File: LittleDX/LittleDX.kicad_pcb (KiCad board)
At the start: 2 copper layers, 140 x 88 mm, 228 parts, among them J1 POWER, J10 PA6, J11 AudioJack2_Dual_Ground_Switch, J12 Conn_Coaxial, J13 Conn_01x01, J14 Conn_01x01, J15 Conn_01x01, J16 Conn_01x01, J17 Filt1, J18 Filt2, J19 AudioJack2_Dual_Ground_Switch, J2 Barrel_Jack, J20 Conn_01x02, J22 Conn_01x02, J23 Conn_01x01, J24 TRANSMIT, J25 Conn_01x04, J26 USB_B, J27 Conn_01x04, J3 Conn_01x01, J4 Conn_01x01, J5 CONFIG, J6 Conn_01x01, J7 Conn_01x01, J8 AudioJack2_Dual_Ground_Switch, J9 PB9, P1 Mini-DIN_6pins_ver4, Q12 MMBT2222, Q13 SS8550, Q14 MMBT3904, Q15 NC, Q3 2N7000, Q4 MMBT3904, Q5 NC, Q6 2N7000, Q7 2N7000, Q8 SS8550, Q9 2N7000, SW1 SW_Push, SW2 SW_Push, SW3 SW_Push, SW4 SW_Push, SW5 SW_Push, SW6 SW_Push, T3 Current, T4 Common-Mode Choke, U1 STM32F103C8Tx, U2 LM78M05_TO252, U3 LM386, U4 AMS1117-3.3, U5 LM358, U6 SI5351A, U7 MicroSD_SPI_CD, U8 Si4735-D60-GU, Y1 8 MHz, Y2 32.768 kHz, Y3 25 MHz

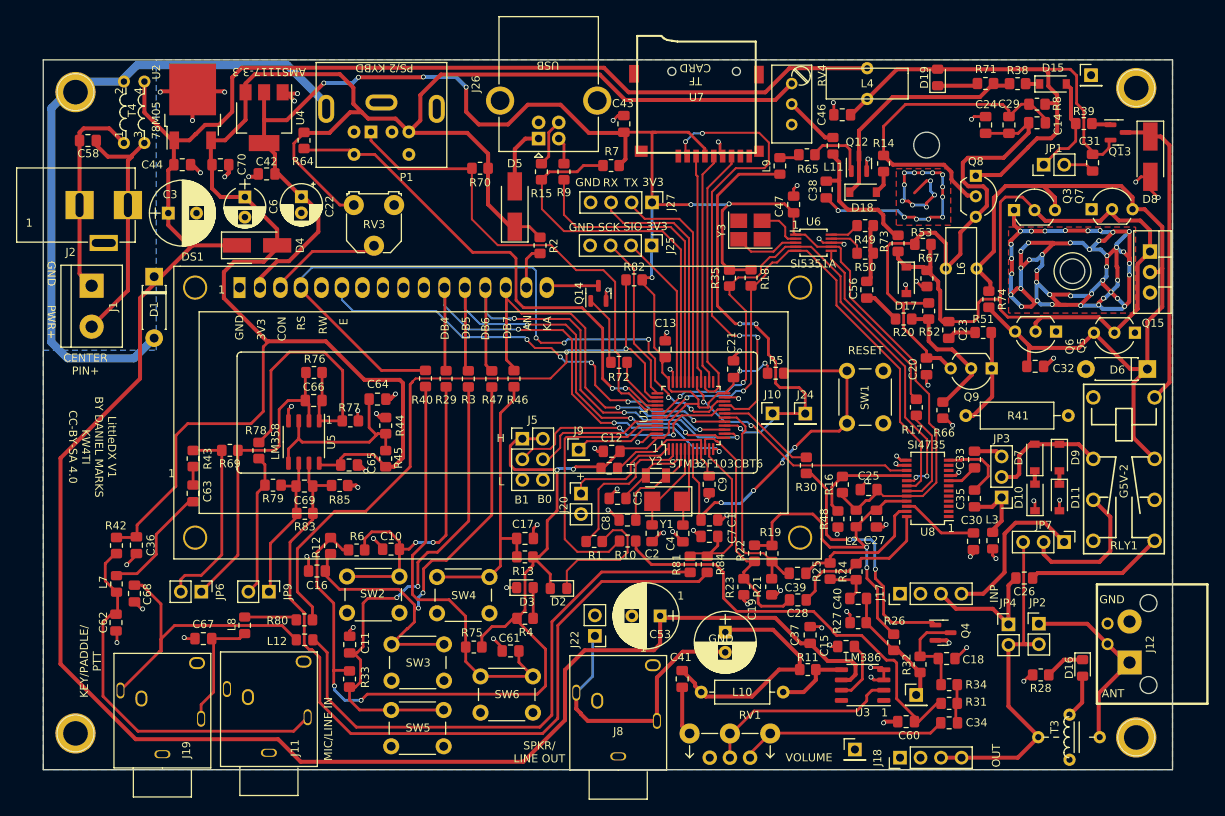
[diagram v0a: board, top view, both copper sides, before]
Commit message: Small moving around of components
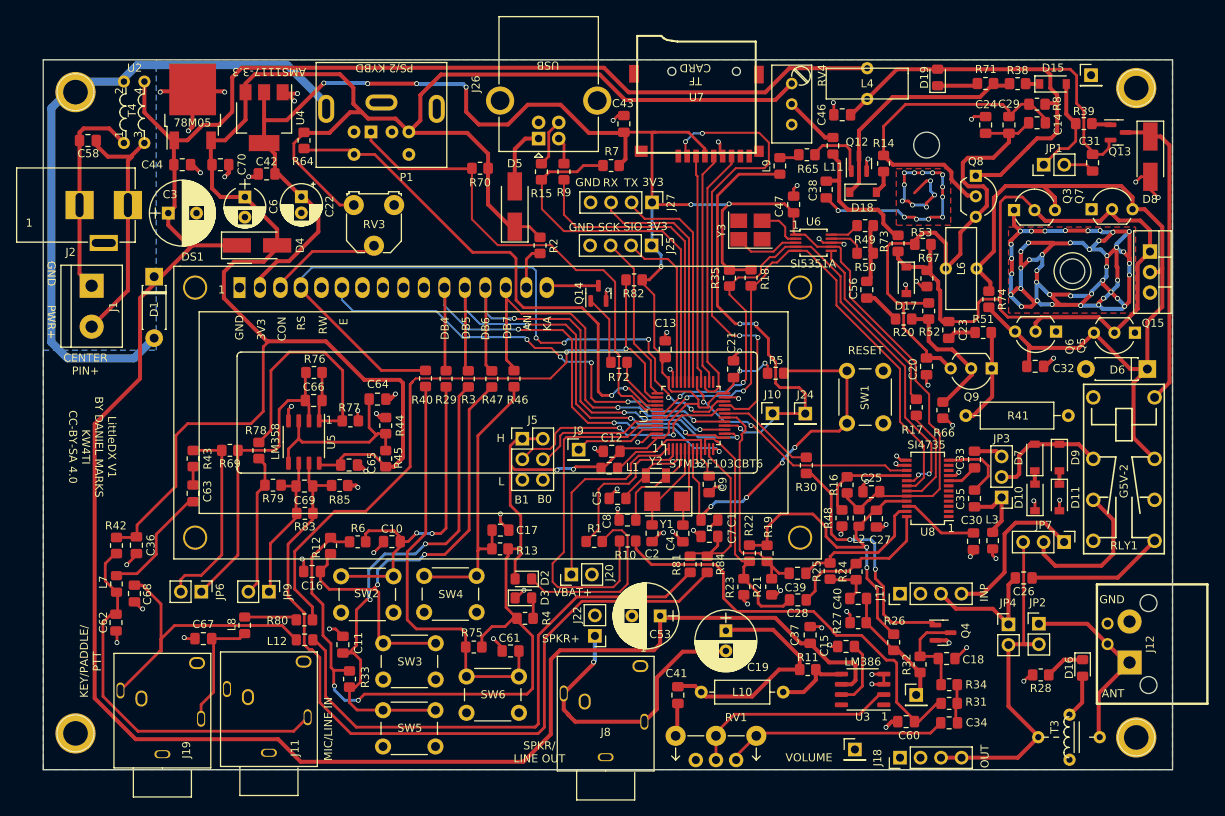
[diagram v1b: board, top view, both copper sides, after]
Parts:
- moved J20 10.1 mm to (115.5, 120.8), turned to 90 degrees
- moved D2 4.52 mm to (109.5, 121.3)
- moved R13 3.24 mm to (106.6, 117.6)
- moved C17 3.22 mm to (106.7, 115.3)
- moved C41 2.07 mm to (128.7, 135.8)
- moved RV1 1.75 mm to (133.4, 143.8)
- moved SW6 1.74 mm to (102.5, 133.4)
- moved SW4 1.60 mm to (97.2, 121.0)
- moved J8 1.56 mm to (119.7, 145.2)
- moved D3 1.29 mm to (109.5, 123.7)
- moved SW3 1.04 mm to (92.2, 129.3)
- moved R6 1.02 mm to (89.0, 116.8)
- moved SW5 1.02 mm to (92.1, 137.6)
- moved C10 0.94 mm to (93.2, 116.7)
- moved C11 0.84 mm to (87.2, 129.5)
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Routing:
- net BEEPOUT: track 32.6 -> 44.4 mm
- net Net-(U1-Pad1): track 14.7 -> 25.2 mm
- net Net-(D2-Pad1): track 16.9 -> 23.1 mm
- net Net-(C14-Pad1): track 69.3 -> 66.2 mm
- net PS2CLK: track 63.7 -> 65.7 mm
- net Net-(C34-Pad2): track 25.7 -> 27.6 mm
- net SPKR: track 35.9 -> 37.6 mm, vias 0 -> 1
- net Net-(J25-Pad2): track 19.3 -> 21.0 mm
- net Net-(RV1-Pad2): track 24.7 -> 26.1 mm
- net +3.3V: track 371.9 -> 370.4 mm
- net Net-(C16-Pad2): track 60.9 -> 59.7 mm
- net E: track 56.6 -> 57.8 mm
- net Net-(D3-Pad2): track 3.82 -> 2.62 mm
- net Net-(JP7-Pad2): track 17.9 -> 19.1 mm
- net GND: track 379.3 -> 380.4 mm
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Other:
- board text added: "SPKR+"
- board text added: "VBAT+"
- board text removed: "+"

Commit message: JLCPCB version 2
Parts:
- removed L1: 100 uH, Inductor_SMD:L_0805_2012Metric_Pad1.15x1.40mm_HandSolder
- added C45: 100 nF, Capacitor_SMD:C_0805_2012Metric_Pad1.18x1.45mm_HandSolder, F.Cu at (107.3, 120.3)
- added C48: 10 uF, Capacitor_SMD:C_0805_2012Metric_Pad1.18x1.45mm_HandSolder, F.Cu at (151.1, 140.1)
- added C49: 100 nF, Capacitor_SMD:C_0805_2012Metric_Pad1.18x1.45mm_HandSolder, F.Cu at (157.9, 128.6)
- added C50: NC, Capacitor_SMD:C_0805_2012Metric_Pad1.18x1.45mm_HandSolder, F.Cu at (162.7, 117.9)
- added C51: NC, Capacitor_SMD:C_0805_2012Metric_Pad1.18x1.45mm_HandSolder, F.Cu at (165.5, 113.8)
- added D12: 1N4148, Diode_SMD:D_SOD-123, F.Cu at (125.5, 120.8)
- added D13: 1N4148, Diode_SMD:D_SOD-123, F.Cu at (139.2, 112.1)
- added D14: 1N4148, Diode_SMD:D_SOD-123, F.Cu at (138.3, 114.8)
- added J21: PB12, Connector_PinHeader_2.54mm:PinHeader_1x01_P2.54mm_Vertical, F.Cu at (132.7, 91.5)
- added R36: 1k, Resistor_SMD:R_0805_2012Metric_Pad1.20x1.40mm_HandSolder, F.Cu at (151.3, 121.9)
- added R37: 1k, Resistor_SMD:R_0805_2012Metric_Pad1.20x1.40mm_HandSolder, F.Cu at (143.6, 121.6)
- added R54: 10k, Resistor_SMD:R_0805_2012Metric_Pad1.20x1.40mm_HandSolder, F.Cu at (151.3, 118.7)
- added R55: 10k, Resistor_SMD:R_0805_2012Metric_Pad1.20x1.40mm_HandSolder, F.Cu at (141.4, 121.6)
- added R56: 47R, Resistor_SMD:R_0805_2012Metric_Pad1.20x1.40mm_HandSolder, F.Cu at (120.4, 107.7)
- added U9: LM358, Package_SO:SOP-8_3.9x4.9mm_P1.27mm, F.Cu at (145.5, 126.3)
- added Y4: 32.768 kHz (NC), Crystal:Crystal_SMD_3215-2Pin_3.2x1.5mm, F.Cu at (165.9, 117.3)
- C27: value 100 nF -> 4.7 uF
- C40: value 4.7 uF -> 100 nF
- C9: value 100 nF -> 10 uF
- D2: footprint Diode_SMD:D_0805_2012Metric_Pad1.15x1.40mm_HandSolder -> LED_SMD:LED_0805_2012Metric_Pad1.15x1.40mm_HandSolder
- R22, R25: value 10k -> 220k
- moved J15 18.6 mm to (169.2, 141.0)
- moved R23 18.2 mm to (153.8, 115.8)
- moved R19 15.7 mm to (151.6, 128.5), turned to 90 degrees
- moved R27 14.7 mm to (137.2, 121.7)
- moved R26 13.9 mm to (151.7, 115.8), turned to 90 degrees
- moved C28 13.7 mm to (156.4, 119.1), turned to -90 degrees
- moved R41 12.3 mm to (164.8, 100.8), turned to 0 degrees
- moved C39 12.2 mm to (152.8, 112.7)
- moved C37 11.6 mm to (143.9, 139.8), turned to -90 degrees
- moved R48 11.0 mm to (153.8, 103.9), turned to 90 degrees
- moved C15 10.5 mm to (147.4, 140.0), turned to -90 degrees
- moved L3 9.60 mm to (165.5, 107.3), turned to 180 degrees
- moved L2 8.64 mm to (148.8, 105.5)
- moved R24 8.56 mm to (153.7, 128.5), turned to -90 degrees
- moved C35 7.35 mm to (165.4, 104.0), turned to 0 degrees
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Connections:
- net Net-(U1-Pad1) renamed VBAT
- C28 pad 2: LCH -> Net-(C28-Pad2)
- C30 pad 1: Net-(C30-Pad1) -> Net-(C27-Pad1)
- C30 pad 2: GND -> Net-(C30-Pad2)
- C39 pad 2: RCH -> Net-(C39-Pad2)
- C40 pad 1: Net-(C40-Pad1) -> +5V
- C40 pad 2: AUDIO -> GND
- R19 pad 1: Net-(C27-Pad1) -> AUDIO
- R19 pad 2: RCH -> Net-(R19-Pad2)
- R21 pad 1: RCH -> Net-(C49-Pad1)
- R22 pad 1: Net-(C27-Pad1) -> Net-(R19-Pad2)
- R22 pad 2: LCH -> Net-(R22-Pad2)
- R23 pad 1: LCH -> Net-(C27-Pad1)
- R23 pad 2: GND -> Net-(C49-Pad1)
- R24 pad 1: Net-(C40-Pad1) -> Net-(R24-Pad1)
- R24 pad 2: Net-(C28-Pad1) -> AUDIO
- R25 pad 1: Net-(C40-Pad1) -> Net-(R24-Pad1)
- R25 pad 2: Net-(C39-Pad1) -> Net-(R25-Pad2)
- R26 pad 1: Net-(C27-Pad1) -> Net-(R25-Pad2)
- R26 pad 2: AUDIO -> Net-(C39-Pad2)
- R27 pad 1: AUDIO -> Net-(C28-Pad2)
- R27 pad 2: GND -> Net-(R22-Pad2)
- U1 pad 25: unconnected-(U1-Pad25) -> Net-(J21-Pad1)
- U3 pad 1: unconnected-(U3-Pad1) -> Net-(C48-Pad1)
- U3 pad 8: unconnected-(U3-Pad8) -> Net-(C48-Pad2)
- U8 pad 22: Net-(C30-Pad1) -> Net-(C30-Pad2)
- U8 pad 3: unconnected-(U8-Pad3) -> Net-(C51-Pad1)
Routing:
- net +5V: track 252.3 -> 392.1 mm, vias 0 -> 2
- net +3.3V: track 370.4 -> 402.7 mm
- net Net-(C49-Pad1): track 0.00 -> 29.8 mm
- net Net-(R19-Pad2): track 0.00 -> 19.4 mm
- net Net-(C28-Pad2): track 0.00 -> 18.8 mm, vias 0 -> 2
- net Net-(R25-Pad2): track 0.00 -> 18.5 mm
- net Net-(C27-Pad1): track 42.6 -> 24.3 mm, vias 2 -> 0
- net Net-(Q4-Pad1): track 31.2 -> 48.8 mm, vias 2 -> 0
- net GND: track 380.4 -> 396.0 mm, vias 136 -> 138
- net Net-(R24-Pad1): track 0.00 -> 14.9 mm
- net Net-(C28-Pad1): track 19.4 -> 4.72 mm
- net Net-(C39-Pad1): track 17.6 -> 3.35 mm
- net Net-(R22-Pad2): track 0.00 -> 11.0 mm
- net Net-(C30-Pad1): track 9.64 -> 0.00 mm
- net RADIORESET: track 31.5 -> 40.2 mm
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
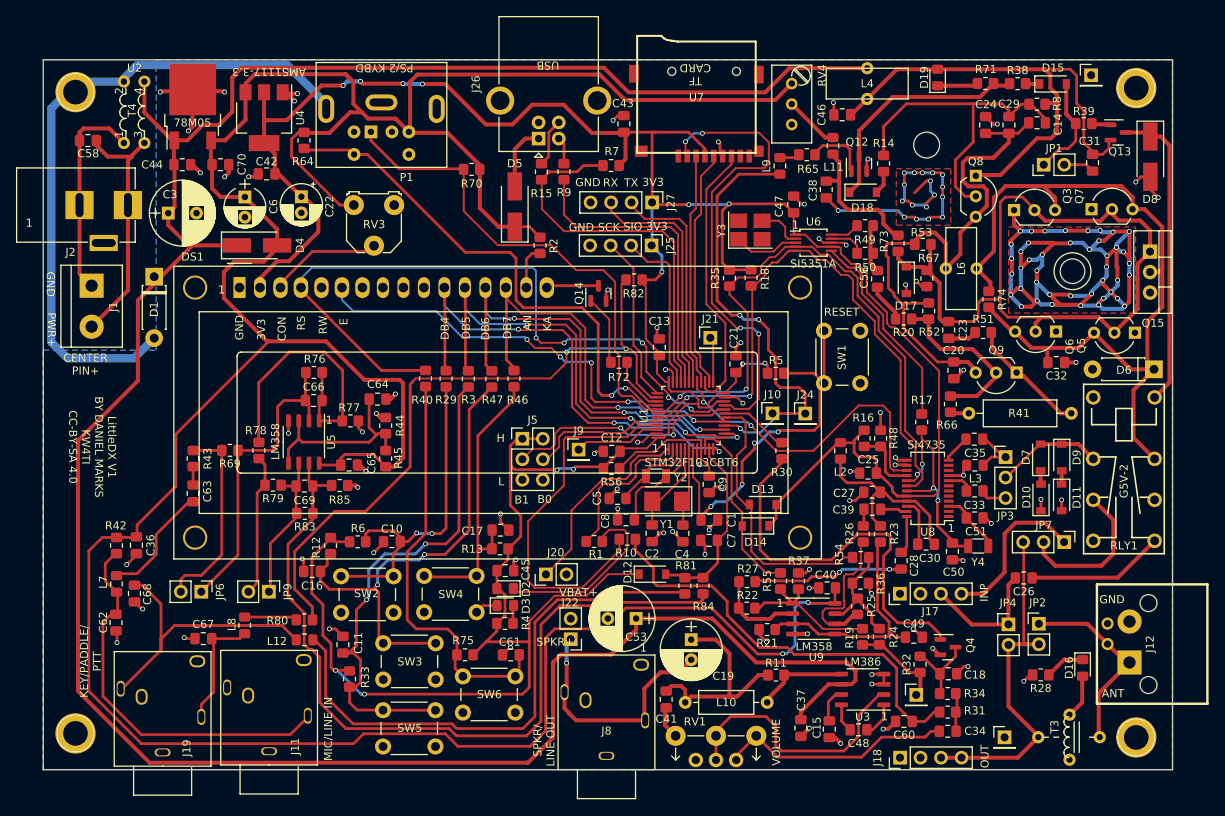
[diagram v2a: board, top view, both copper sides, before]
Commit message: Revised JLCPCB order: added negative LCD voltage supply
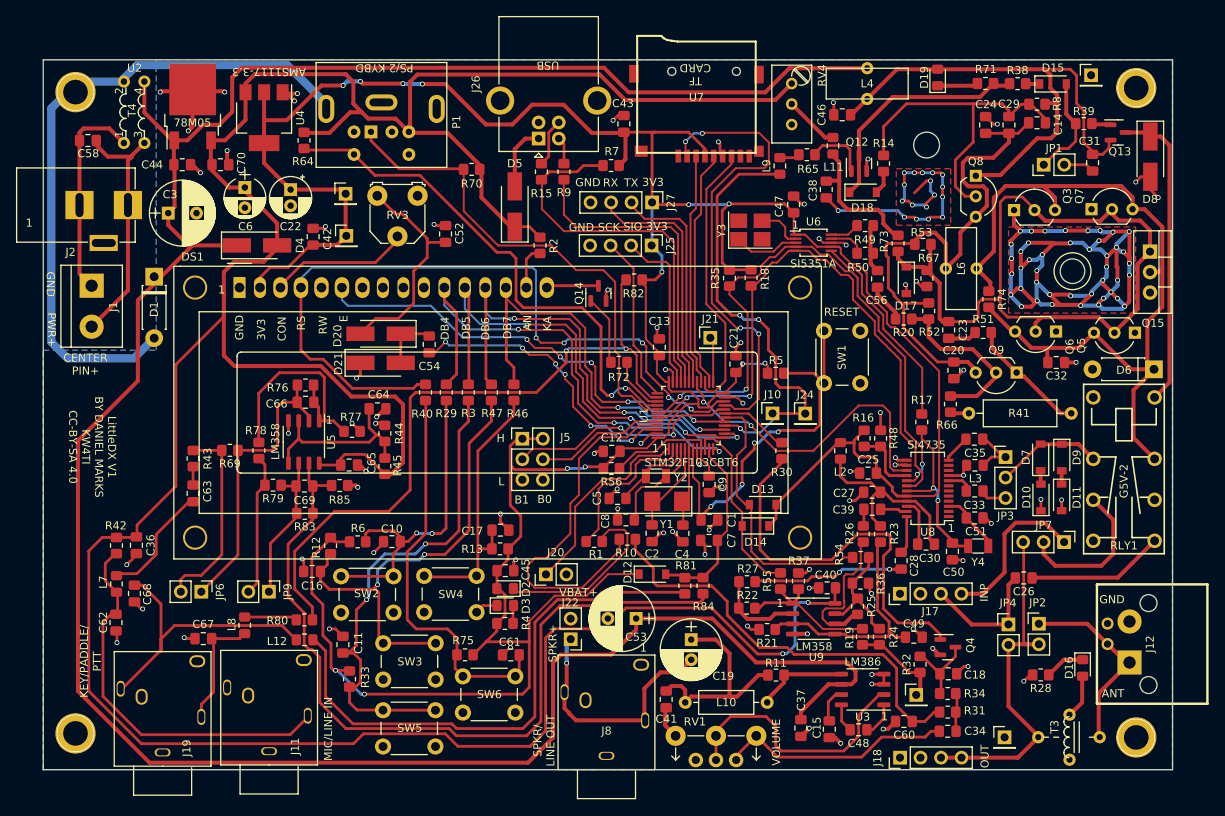
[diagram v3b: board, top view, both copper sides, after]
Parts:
- added C52: 1 uF, Capacitor_SMD:C_0805_2012Metric_Pad1.18x1.45mm_HandSolder, F.Cu at (99.9, 78.6)
- added C54: 1 uF, Capacitor_SMD:C_0805_2012Metric_Pad1.18x1.45mm_HandSolder, F.Cu at (97.8, 92.3)
- added D20: SS14, Diode_SMD:D_SMA_Handsoldering, F.Cu at (91.8, 91.0)
- added D21: SS14, Diode_SMD:D_SMA_Handsoldering, F.Cu at (91.8, 94.6)
- added J28: PS, Connector_PinHeader_2.54mm:PinHeader_1x01_P2.54mm_Vertical, F.Cu at (87.6, 78.8)
- J9: value PB9 -> PS
- moved J9 42.9 mm to (87.5, 73.6)
- moved C42 9.69 mm to (83.5, 78.9), turned to 90 degrees
- moved RV3 3.13 mm to (96.4, 73.8)
- moved R76 1.88 mm to (82.5, 97.3)
- moved R40 1.73 mm to (97.4, 98.2)
- moved R46 1.70 mm to (108.4, 98.2)
- moved R29 1.69 mm to (100.0, 98.2)
- moved R3 1.68 mm to (102.7, 98.2)
- moved R47 1.67 mm to (105.6, 98.2)
- moved C22 1.60 mm to (80.7, 73.1)
- moved R77 1.31 mm to (88.3, 103.1)
- moved C64 1.20 mm to (91.4, 100.3)
- moved C6 1.17 mm to (75.0, 72.8)
- moved C66 1.04 mm to (82.5, 99.5)
- moved R44 0.97 mm to (92.3, 103.3)
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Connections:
- J9 pad 1: Net-(J9-Pad1) -> +3.3V
- RV3 pad 3: +5V -> Net-(RV3-Pad3)
- U1 pad 46: Net-(J9-Pad1) -> PB9G
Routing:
- net PB9G: track 0.00 -> 36.6 mm, vias 0 -> 6
- net Net-(RV3-Pad3): track 0.00 -> 27.6 mm
- net Net-(J9-Pad1): track 10.8 -> 0.00 mm
- net +5V: track 392.1 -> 383.7 mm
- net +3.3V: track 402.7 -> 411.1 mm
- net Net-(C54-Pad2): track 0.00 -> 7.24 mm
- net Net-(C66-Pad2): track 35.6 -> 29.4 mm
- net RS: track 89.5 -> 95.0 mm
- net Net-(DS1-Pad3): track 14.0 -> 17.6 mm
- net GND: track 396.0 -> 399.2 mm, vias 138 -> 140
- net Net-(C66-Pad1): track 39.3 -> 37.0 mm
- net DB4: track 60.0 -> 62.1 mm
- net Net-(C61-Pad2): track 51.6 -> 49.8 mm
- net Net-(C17-Pad2): track 36.3 -> 34.6 mm
- net Net-(C16-Pad2): track 59.7 -> 58.0 mm
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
